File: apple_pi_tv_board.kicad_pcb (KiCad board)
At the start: 2 copper layers, 61 x 85.1 mm, 7 parts, among them J1 RJ45, U1 HDMI/USB, U2 apple tv tos link

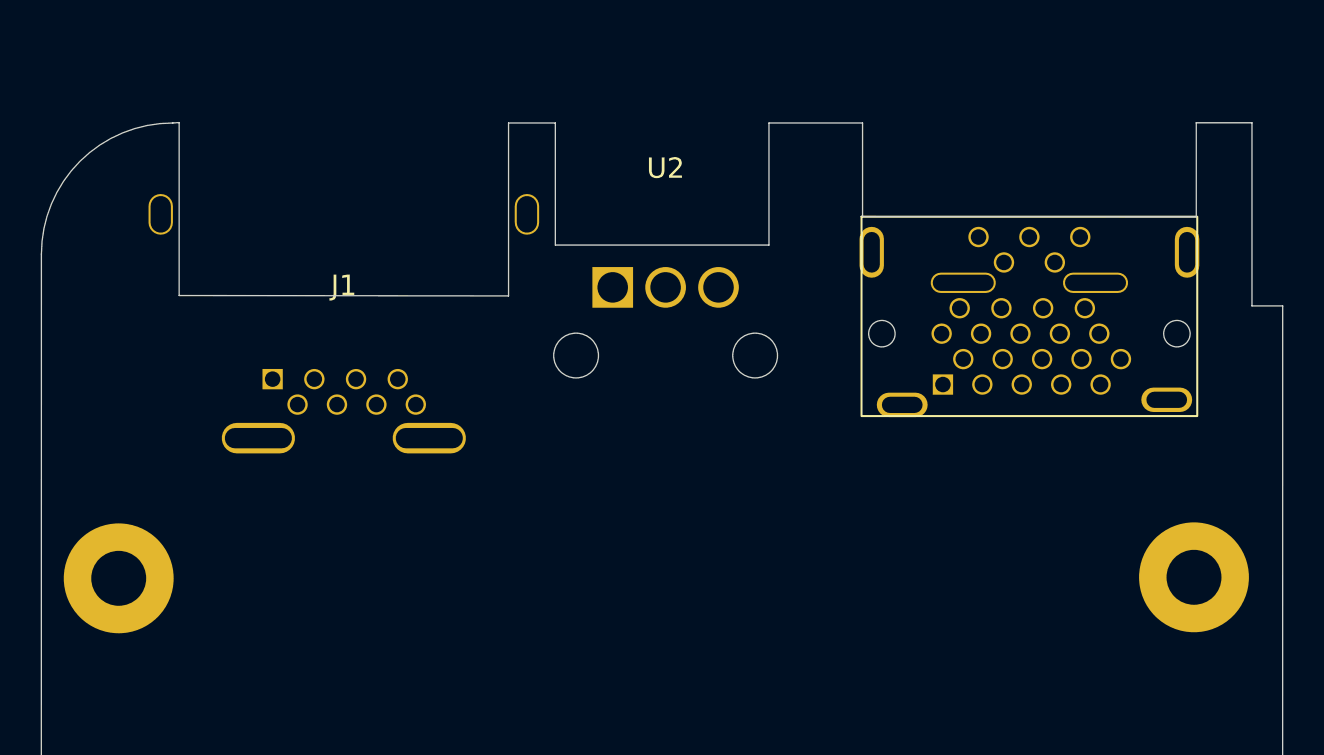
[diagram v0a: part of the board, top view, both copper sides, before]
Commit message: moved the parts slightly
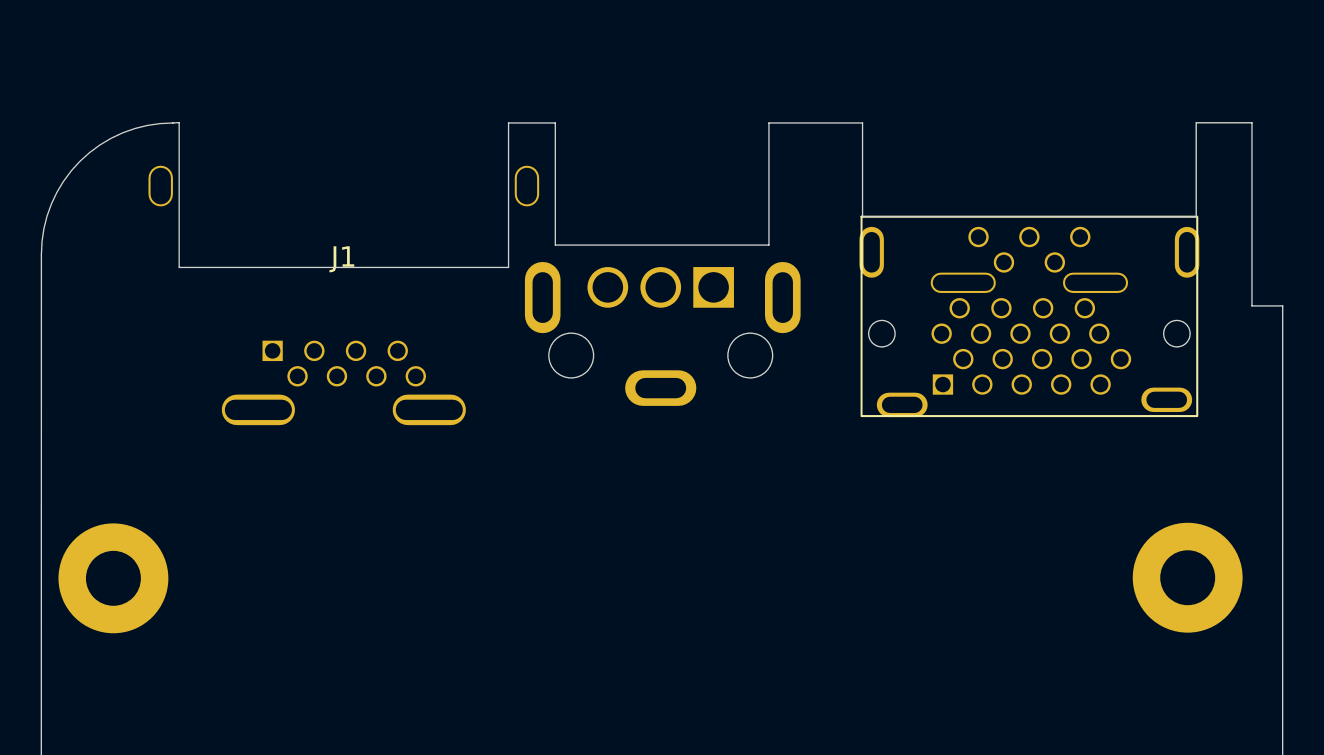
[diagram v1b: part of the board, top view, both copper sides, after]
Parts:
- U2: moved to B.Cu
- moved J1 1.39 mm to (91.7, 77.8)
- moved H1 0.31 mm to (133.2, 93.0)
- moved H2 0.26 mm to (80.4, 93.0)
- moved U2 0.24 mm to (107.3, 76.7), turned to 180 degrees
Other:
- outline, holes or cut-outs redrawn
